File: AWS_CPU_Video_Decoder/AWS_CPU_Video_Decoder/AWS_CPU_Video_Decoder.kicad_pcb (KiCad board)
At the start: 2 copper layers, 132 x 99.6 mm, 176 parts, among them J1 Conn_02x20_Odd_Even, J10 Conn_01x04_Pin, J11 Conn_01x04_Pin, J12 Conn_01x04_Pin, J13 Conn_01x04_Pin, J14 Conn_01x04_Pin, J15 Conn_01x04_Pin, J16 Video, J18 Conn_01x02_Pin, J19 Conn_01x02_Pin, J2 Conn_01x04_Pin, J3 Video, J4 Conn_01x04_Pin, J5 Conn_02x20_Odd_Even, J6 Conn_01x04_Pin, J7 Conn_01x04_Pin, J8 Conn_01x04_Pin, J9 Conn_01x04_Pin, SW1 Reset

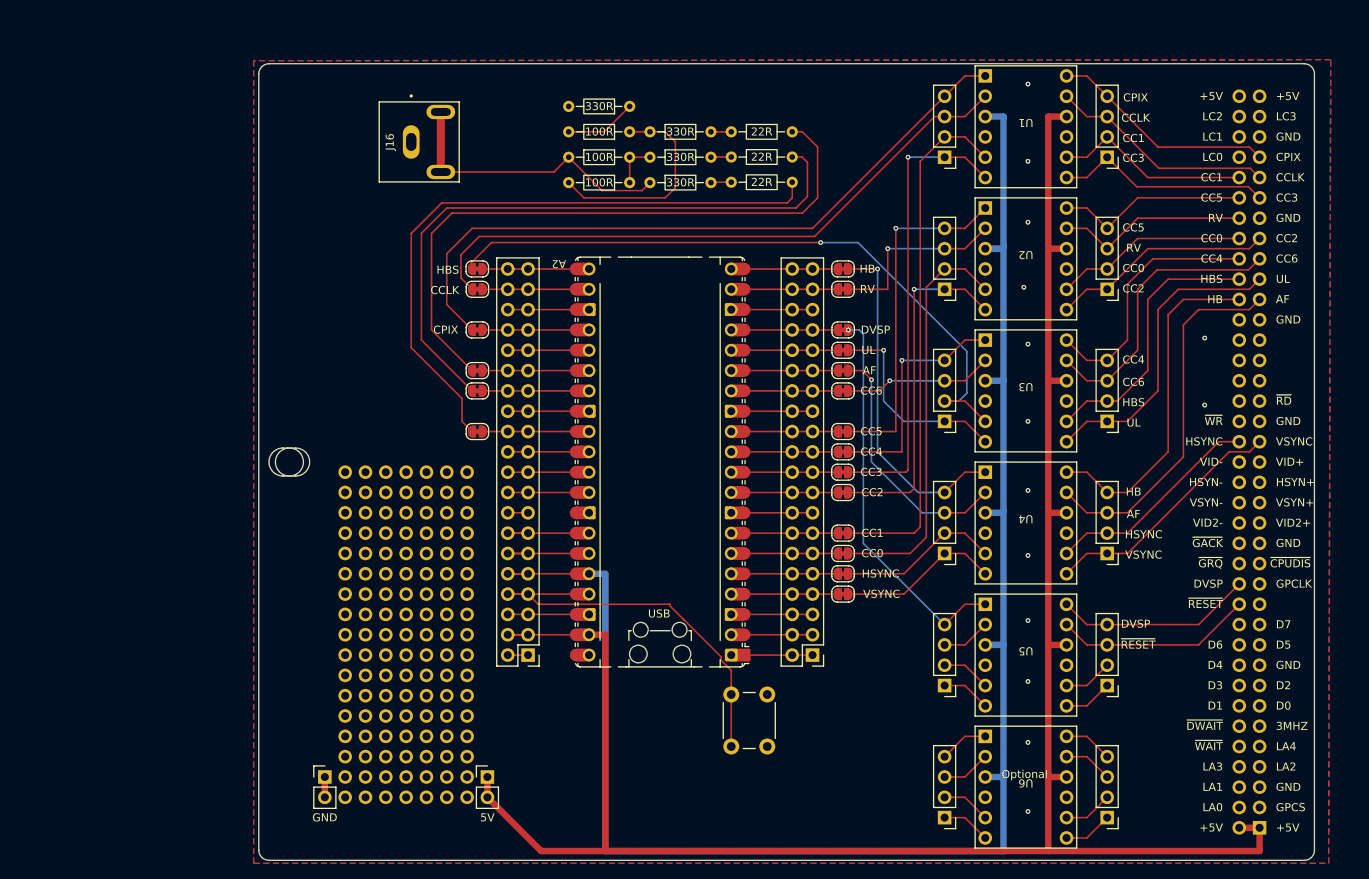
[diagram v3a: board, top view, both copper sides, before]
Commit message: Added Schottky Diode
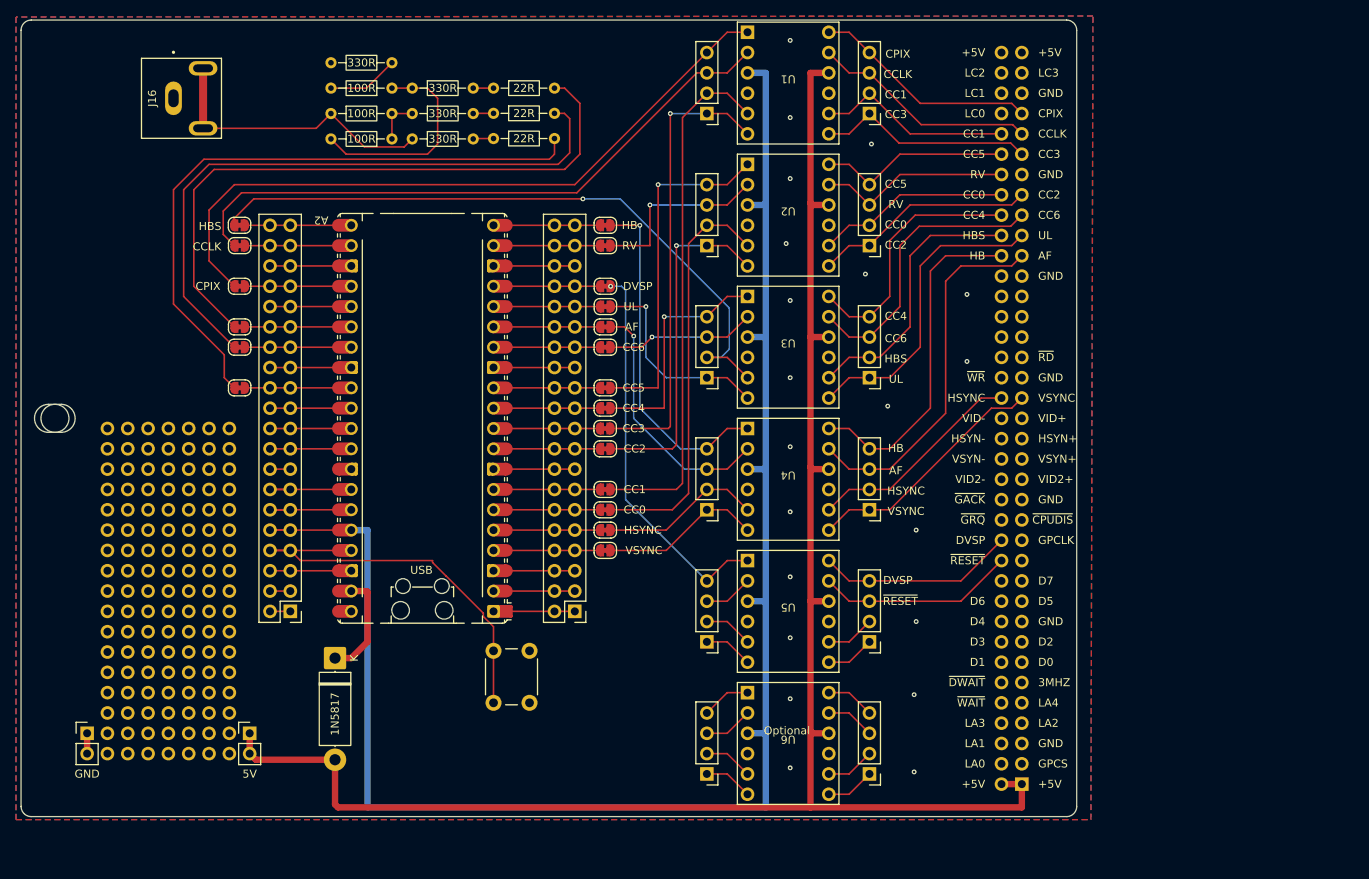
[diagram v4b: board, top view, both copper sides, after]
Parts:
- added D1: 1N5817, Diode_THT:D_5W_P12.70mm_Horizontal, F.Cu at (118.1, 126.1)
- moved ? 30.2 mm to (102.4, 122.8)
- moved ? 30.2 mm to (102.4, 115.2)
- moved ? 30.2 mm to (102.4, 133.0)
- moved ? 30.2 mm to (102.4, 135.5)
- moved JP8 30.2 mm to (151.9, 92.3)
- moved ? 30.2 mm to (102.4, 110.1)
- moved ? 30.2 mm to (102.4, 97.4)
- moved ? 30.2 mm to (102.4, 99.9)
- moved ? 30.2 mm to (102.4, 112.6)
- moved ? 30.2 mm to (102.4, 127.9)
- moved ? 30.2 mm to (102.4, 117.7)
- moved ? 30.2 mm to (102.4, 130.4)
- moved ? 30.2 mm to (102.4, 102.5)
- moved ? 30.2 mm to (102.4, 120.3)
- moved ? 30.2 mm to (102.4, 105.0)
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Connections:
- A2 pad 39: +5V -> Net-(A2-VSYS)
- J1 pad 3: +5V -> unconnected-(J1-Pin_3-Pad3)
- J1 pad 4: +5V -> unconnected-(J1-Pin_3-Pad3)
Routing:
- net +5V: track 254.9 -> 216.4 mm
- net Net-(A2-VSYS): track 0.00 -> 13.2 mm
- net Net-(J16-In): track 28.3 -> 35.8 mm
- net unconnected-(J1-Pin_3-Pad3): track 0.00 -> 2.54 mm
- net GND: vias 14 -> 21
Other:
- outline, holes or cut-outs redrawn
